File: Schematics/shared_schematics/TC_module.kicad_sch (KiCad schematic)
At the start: 12 parts, among them J7 Screw_Terminal_01x02

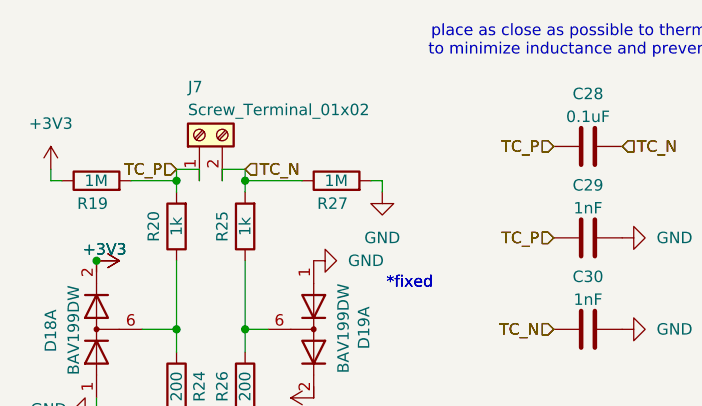
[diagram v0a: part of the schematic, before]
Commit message: organize working copy of lower valve board for merge to main
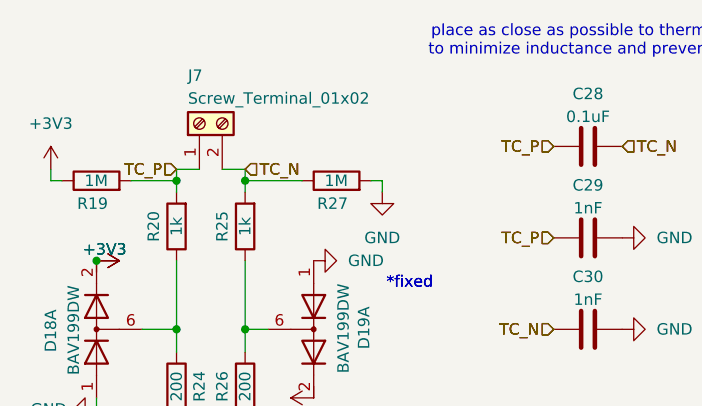
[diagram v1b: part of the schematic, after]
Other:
- moved on the sheet: J7
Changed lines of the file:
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@@
-	(wire
-		(pts
-			(xy 153.67 80.01) (xy 153.67 81.28)
-		)
-		(stroke
-			(width 0)
-			(type default)
-		)
-	)
-	(wire
-		(pts
-			(xy 151.13 80.01) (xy 151.13 81.28)
-		)
-		(stroke
-			(width 0)
-			(type default)
-		)
-	)
 	(wire
 		(pts
@@
 		(shape input)
 		(at 148.59 80.01 180)
-		(fields_autoplaced yes)
 		(effects
 			(font
@@
 		(shape input)
 		(at 190.5 77.47 180)
-		(fields_autoplaced yes)
 		(effects
 			(font
@@
 		(shape input)
 		(at 190.5 77.47 180)
-		(fields_autoplaced yes)
 		(effects
 			(font
@@
 		(shape input)
 		(at 148.59 114.3 180)
-		(fields_autoplaced yes)
 		(effects
 			(font
@@
 		(shape input)
 		(at 198.12 77.47 0)
-		(fields_autoplaced yes)
 		(effects
 			(font
@@
 		(shape input)
 		(at 190.5 87.63 180)
-		(fields_autoplaced yes)
 		(effects
 			(font
@@
 		(shape input)
 		(at 148.59 114.3 180)
-		(fields_autoplaced yes)
 		(effects
 			(font
@@
 		(shape input)
 		(at 190.5 97.79 180)
-		(fields_autoplaced yes)
 		(effects
 			(font
@@
 		(shape input)
 		(at 190.5 87.63 180)
-		(fields_autoplaced yes)
 		(effects
 			(font
@@
 		(shape input)
 		(at 148.59 80.01 180)
-		(fields_autoplaced yes)
 		(effects
 			(font
@@
 		(shape input)
 		(at 198.12 77.47 0)
-		(fields_autoplaced yes)
 		(effects
 			(font
@@
 		(shape input)
 		(at 156.21 80.01 0)
-		(fields_autoplaced yes)
 		(effects
 			(font
@@
 		(shape input)
 		(at 156.21 114.3 0)
-		(fields_autoplaced yes)
 		(effects
 			(font
@@
 		(shape input)
 		(at 190.5 97.79 180)
-		(fields_autoplaced yes)
 		(effects
 			(font
@@
 		(shape input)
 		(at 156.21 80.01 0)
-		(fields_autoplaced yes)
 		(effects
 			(font
@@
 		(shape input)
 		(at 156.21 114.3 0)
-		(fields_autoplaced yes)
 		(effects
 			(font
@@
 				)
 			)
-			(project ""
+			(project "lower_lc_board"
 				(path "/d63798c4-e363-437e-9012-e4aff32e6642/c6419db7-28a9-4bfa-8244-fc88166c795c/0f673b05-1261-4d55-8b13-e3d5496cfefa"
 					(reference "#PWR0118")
@@
 				)
 			)
-			(project ""
+			(project "lower_lc_board"
 				(path "/d63798c4-e363-437e-9012-e4aff32e6642/c6419db7-28a9-4bfa-8244-fc88166c795c/0f673b05-1261-4d55-8b13-e3d5496cfefa"
 					(reference "R26")
@@
 				)
 			)
-			(project ""
+			(project "lower_lc_board"
 				(path "/d63798c4-e363-437e-9012-e4aff32e6642/c6419db7-28a9-4bfa-8244-fc88166c795c/0f673b05-1261-4d55-8b13-e3d5496cfefa"
 					(reference "R24")
@@
 				)
 			)
-			(project ""
+			(project "lower_lc_board"
 				(path "/d63798c4-e363-437e-9012-e4aff32e6642/c6419db7-28a9-4bfa-8244-fc88166c795c/0f673b05-1261-4d55-8b13-e3d5496cfefa"
 					(reference "C32")
@@
 				)
 			)
-			(project ""
+			(project "lower_lc_board"
 				(path "/d63798c4-e363-437e-9012-e4aff32e6642/c6419db7-28a9-4bfa-8244-fc88166c795c/0f673b05-1261-4d55-8b13-e3d5496cfefa"
 					(reference "R27")
@@
 				)
 			)
-			(project ""
+			(project "lower_lc_board"
 				(path "/d63798c4-e363-437e-9012-e4aff32e6642/c6419db7-28a9-4bfa-8244-fc88166c795c/0f673b05-1261-4d55-8b13-e3d5496cfefa"
 					(reference "C31")
@@
 				)
 			)
-			(project ""
+			(project "lower_lc_board"
 				(path "/d63798c4-e363-437e-9012-e4aff32e6642/c6419db7-28a9-4bfa-8244-fc88166c795c/0f673b05-1261-4d55-8b13-e3d5496cfefa"
 					(reference "R40")
@@
 			)
 		)
-		(property "Datasheet" "${KIPRJMOD}/../../Documentation/diode_BAV16WS_DS.pdf"
+		(property "Datasheet" "${KIPRJMOD}/../../Datasheets/diode_BAV16WS_DS.pdf"
 			(at 163.83 97.79 0)
 			(effects
@@
 				)
 			)
-			(project ""
+			(project "lower_lc_board"
 				(path "/d63798c4-e363-437e-9012-e4aff32e6642/c6419db7-28a9-4bfa-8244-fc88166c795c/0f673b05-1261-4d55-8b13-e3d5496cfefa"
 					(reference "D18")
@@
 			)
 		)
-		(property "Datasheet" "${KIPRJMOD}/../../Documentation/diode_BAV16WS_DS.pdf"
+		(property "Datasheet" "${KIPRJMOD}/../../Datasheets/diode_BAV16WS_DS.pdf"
 			(at 139.7 97.79 0)
 			(effects
@@
 				)
 			)
-			(project ""
+			(project "lower_lc_board"
 				(path "/d63798c4-e363-437e-9012-e4aff32e6642/c6419db7-28a9-4bfa-8244-fc88166c795c/0f673b05-1261-4d55-8b13-e3d5496cfefa"
 					(reference "D18")
@@
 				)
 			)
-			(project ""
+			(project "lower_lc_board"
 				(path "/d63798c4-e363-437e-9012-e4aff32e6642/c6419db7-28a9-4bfa-8244-fc88166c795c/0f673b05-1261-4d55-8b13-e3d5496cfefa"
 					(reference "#PWR0114")
@@
 				)
 			)
-			(project ""
+			(project "lower_lc_board"
 				(path "/d63798c4-e363-437e-9012-e4aff32e6642/c6419db7-28a9-4bfa-8244-fc88166c795c/0f673b05-1261-4d55-8b13-e3d5496cfefa"
 					(reference "R29")
@@
 				)
 			)
-			(project ""
+			(project "lower_lc_board"
 				(path "/d63798c4-e363-437e-9012-e4aff32e6642/c6419db7-28a9-4bfa-8244-fc88166c795c/0f673b05-1261-4d55-8b13-e3d5496cfefa"
 					(reference "#PWR0120")
@@
 				)
 			)
-			(project ""
+			(project "lower_lc_board"
 				(path "/d63798c4-e363-437e-9012-e4aff32e6642/c6419db7-28a9-4bfa-8244-fc88166c795c/0f673b05-1261-4d55-8b13-e3d5496cfefa"
 					(reference "R28")
@@
 				)
 			)
-			(project ""
+			(project "lower_lc_board"
 				(path "/d63798c4-e363-437e-9012-e4aff32e6642/c6419db7-28a9-4bfa-8244-fc88166c795c/0f673b05-1261-4d55-8b13-e3d5496cfefa"
 					(reference "C30")
@@
 	(symbol
 		(lib_id "Connector:Screw_Terminal_01x02")
-		(at 151.13 76.2 90)
+		(at 151.13 74.93 90)
 		(unit 1)
 		(exclude_from_sim no)
@@
 		(dnp no)
 		(property "Reference" "J7"
-			(at 149.86 70.866 90)
+			(at 149.86 69.596 90)
 			(effects
 				(font
@@
 		)
 		(property "Value" "Screw_Terminal_01x02"
-			(at 149.86 73.406 90)
+			(at 149.86 72.136 90)
 			(effects
 				(font
@@
 		)
 		(property "Footprint" "TerminalBlock_TE-Connectivity:TerminalBlock_TE_282834-2_1x02_P2.54mm_Horizontal"
-			(at 151.13 76.2 0)
+			(at 151.13 74.93 0)
 			(effects
 				(font
@@
 		)
 		(property "Datasheet" "~"
-			(at 151.13 76.2 0)
+			(at 151.13 74.93 0)
 			(effects
 				(font
@@
 		)
 		(property "Description" "Generic screw terminal, single row, 01x02, script generated (kicad-library-utils/schlib/autogen/connector/)"
-			(at 151.13 76.2 0)
+			(at 151.13 74.93 0)
 			(effects
 				(font
@@
 		)
 		(property "Digikey" "ED10561-ND"
-			(at 151.13 76.2 90)
+			(at 151.13 74.93 90)
 			(effects
 				(font
@@
 				)
 			)
-			(project ""
+			(project "lower_lc_board"
 				(path "/d63798c4-e363-437e-9012-e4aff32e6642/c6419db7-28a9-4bfa-8244-fc88166c795c/0f673b05-1261-4d55-8b13-e3d5496cfefa"
 					(reference "J7")
@@
 				)
 			)
-			(project ""
+			(project "lower_lc_board"
 				(path "/d63798c4-e363-437e-9012-e4aff32e6642/c6419db7-28a9-4bfa-8244-fc88166c795c/0f673b05-1261-4d55-8b13-e3d5496cfefa"
 					(reference "#PWR0129")

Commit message: lower refactor for review
 - curr using horziontal screw for TC
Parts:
- C28: footprint Capacitor_SMD:C_0805_2012Metric -> Capacitor_SMD:C_0603_1608Metric; JLCPCB C49678 -> C14663
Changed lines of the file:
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@@
 		(shape input)
 		(at 148.59 80.01 180)
+		(fields_autoplaced yes)
 		(effects
 			(font
@@
 		(shape input)
 		(at 190.5 77.47 180)
+		(fields_autoplaced yes)
 		(effects
 			(font
@@
 		(shape input)
 		(at 190.5 77.47 180)
+		(fields_autoplaced yes)
 		(effects
 			(font
@@
 		(shape input)
 		(at 148.59 114.3 180)
+		(fields_autoplaced yes)
 		(effects
 			(font
@@
 		(shape input)
 		(at 198.12 77.47 0)
+		(fields_autoplaced yes)
 		(effects
 			(font
@@
 		(shape input)
 		(at 190.5 87.63 180)
+		(fields_autoplaced yes)
 		(effects
 			(font
@@
 		(shape input)
 		(at 148.59 114.3 180)
+		(fields_autoplaced yes)
 		(effects
 			(font
@@
 		(shape input)
 		(at 190.5 97.79 180)
+		(fields_autoplaced yes)
 		(effects
 			(font
@@
 		(shape input)
 		(at 190.5 87.63 180)
+		(fields_autoplaced yes)
 		(effects
 			(font
@@
 		(shape input)
 		(at 148.59 80.01 180)
+		(fields_autoplaced yes)
 		(effects
 			(font
@@
 		(shape input)
 		(at 198.12 77.47 0)
+		(fields_autoplaced yes)
 		(effects
 			(font
@@
 		(shape input)
 		(at 156.21 80.01 0)
+		(fields_autoplaced yes)
 		(effects
 			(font
@@
 		(shape input)
 		(at 156.21 114.3 0)
+		(fields_autoplaced yes)
 		(effects
 			(font
@@
 		(shape input)
 		(at 190.5 97.79 180)
+		(fields_autoplaced yes)
 		(effects
 			(font
@@
 		(shape input)
 		(at 156.21 80.01 0)
+		(fields_autoplaced yes)
 		(effects
 			(font
@@
 		(shape input)
 		(at 156.21 114.3 0)
+		(fields_autoplaced yes)
 		(effects
 			(font
@@
 					(unit 1)
 				)
-				(path "/d63798c4-e363-437e-9012-e4aff32e6642/c6419db7-28a9-4bfa-8244-fc88166c795c/a028da42-e7da-423c-a83c-32336e9b7a16"
-					(reference "#PWR0103")
-					(unit 1)
-				)
 			)
 		)
@@
 					(unit 1)
 				)
-				(path "/d63798c4-e363-437e-9012-e4aff32e6642/c6419db7-28a9-4bfa-8244-fc88166c795c/a028da42-e7da-423c-a83c-32336e9b7a16"
-					(reference "#PWR0110")
-					(unit 1)
-				)
 			)
 		)
@@
 					(unit 1)
 				)
-				(path "/d63798c4-e363-437e-9012-e4aff32e6642/c6419db7-28a9-4bfa-8244-fc88166c795c/a028da42-e7da-423c-a83c-32336e9b7a16"
-					(reference "R54")
-					(unit 1)
-				)
 			)
 		)
@@
 					(unit 1)
 				)
-				(path "/d63798c4-e363-437e-9012-e4aff32e6642/c6419db7-28a9-4bfa-8244-fc88166c795c/a028da42-e7da-423c-a83c-32336e9b7a16"
-					(reference "R55")
-					(unit 1)
-				)
 			)
 		)
@@
 					(unit 1)
 				)
-				(path "/d63798c4-e363-437e-9012-e4aff32e6642/c6419db7-28a9-4bfa-8244-fc88166c795c/a028da42-e7da-423c-a83c-32336e9b7a16"
-					(reference "C55")
-					(unit 1)
-				)
 			)
 		)
@@
 					(unit 1)
 				)
-				(path "/d63798c4-e363-437e-9012-e4aff32e6642/c6419db7-28a9-4bfa-8244-fc88166c795c/a028da42-e7da-423c-a83c-32336e9b7a16"
-					(reference "R59")
-					(unit 1)
-				)
 			)
 		)
@@
 					(unit 1)
 				)
-				(path "/d63798c4-e363-437e-9012-e4aff32e6642/c6419db7-28a9-4bfa-8244-fc88166c795c/a028da42-e7da-423c-a83c-32336e9b7a16"
-					(reference "#PWR0119")
-					(unit 1)
-				)
 			)
 		)
@@
 					(unit 1)
 				)
-				(path "/d63798c4-e363-437e-9012-e4aff32e6642/c6419db7-28a9-4bfa-8244-fc88166c795c/a028da42-e7da-423c-a83c-32336e9b7a16"
-					(reference "C54")
-					(unit 1)
-				)
 			)
 		)
@@
 					(unit 1)
 				)
-				(path "/d63798c4-e363-437e-9012-e4aff32e6642/c6419db7-28a9-4bfa-8244-fc88166c795c/a028da42-e7da-423c-a83c-32336e9b7a16"
-					(reference "R58")
-					(unit 1)
-				)
 			)
 		)
@@
 					(unit 2)
 				)
-				(path "/d63798c4-e363-437e-9012-e4aff32e6642/c6419db7-28a9-4bfa-8244-fc88166c795c/a028da42-e7da-423c-a83c-32336e9b7a16"
-					(reference "D9")
-					(unit 2)
-				)
 			)
 		)
@@
 					(unit 1)
 				)
-				(path "/d63798c4-e363-437e-9012-e4aff32e6642/c6419db7-28a9-4bfa-8244-fc88166c795c/a028da42-e7da-423c-a83c-32336e9b7a16"
-					(reference "D9")
-					(unit 1)
-				)
 			)
 		)
@@
 					(unit 1)
 				)
-				(path "/d63798c4-e363-437e-9012-e4aff32e6642/c6419db7-28a9-4bfa-8244-fc88166c795c/a028da42-e7da-423c-a83c-32336e9b7a16"
-					(reference "#PWR094")
-					(unit 1)
-				)
 			)
 		)
@@
 					(unit 1)
 				)
-				(path "/d63798c4-e363-437e-9012-e4aff32e6642/c6419db7-28a9-4bfa-8244-fc88166c795c/a028da42-e7da-423c-a83c-32336e9b7a16"
-					(reference "#PWR0138")
-					(unit 1)
-				)
 			)
 		)
@@
 					(unit 1)
 				)
-				(path "/d63798c4-e363-437e-9012-e4aff32e6642/c6419db7-28a9-4bfa-8244-fc88166c795c/a028da42-e7da-423c-a83c-32336e9b7a16"
-					(reference "R56")
-					(unit 1)
-				)
 			)
 		)
@@
 					(unit 1)
 				)
-				(path "/d63798c4-e363-437e-9012-e4aff32e6642/c6419db7-28a9-4bfa-8244-fc88166c795c/a028da42-e7da-423c-a83c-32336e9b7a16"
-					(reference "#PWR0100")
-					(unit 1)
-				)
 			)
 		)
@@
 					(unit 1)
 				)
-				(path "/d63798c4-e363-437e-9012-e4aff32e6642/c6419db7-28a9-4bfa-8244-fc88166c795c/a028da42-e7da-423c-a83c-32336e9b7a16"
-					(reference "#PWR098")
-					(unit 1)
-				)
 			)
 		)
@@
 					(unit 1)
 				)
-				(path "/d63798c4-e363-437e-9012-e4aff32e6642/c6419db7-28a9-4bfa-8244-fc88166c795c/a028da42-e7da-423c-a83c-32336e9b7a16"
-					(reference "R57")
-					(unit 1)
-				)
 			)
 		)
@@
 					(unit 1)
 				)
-				(path "/d63798c4-e363-437e-9012-e4aff32e6642/c6419db7-28a9-4bfa-8244-fc88166c795c/a028da42-e7da-423c-a83c-32336e9b7a16"
-					(reference "#PWR096")
-					(unit 1)
-				)
 			)
 		)
@@
 			)
 		)
-		(property "Footprint" "Capacitor_SMD:C_0805_2012Metric"
+		(property "Footprint" "Capacitor_SMD:C_0603_1608Metric"
 			(at 190.5 78.4352 0)
 			(effects
@@
 			)
 		)
-		(property "JLCPCB" "C49678"
+		(property "JLCPCB" "C14663"
 			(at 194.31 77.47 0)
 			(effects
@@
 				(path "/d63798c4-e363-437e-9012-e4aff32e6642/c6419db7-28a9-4bfa-8244-fc88166c795c/0f673b05-1261-4d55-8b13-e3d5496cfefa"
 					(reference "C30")
-					(unit 1)
-				)
-				(path "/d63798c4-e363-437e-9012-e4aff32e6642/c6419db7-28a9-4bfa-8244-fc88166c795c/a028da42-e7da-423c-a83c-32336e9b7a16"
-					(reference "C53")
 					(unit 1)
 				)
@@
 					(unit 1)
 				)
-				(path "/d63798c4-e363-437e-9012-e4aff32e6642/c6419db7-28a9-4bfa-8244-fc88166c795c/a028da42-e7da-423c-a83c-32336e9b7a16"
-					(reference "J11")
-					(unit 1)
-				)
 			)
 		)
@@
 					(unit 1)
 				)
-				(path "/d63798c4-e363-437e-9012-e4aff32e6642/c6419db7-28a9-4bfa-8244-fc88166c795c/a028da42-e7da-423c-a83c-32336e9b7a16"
-					(reference "#PWR0107")
-					(unit 1)
-				)

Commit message: update with new TC screw terminal
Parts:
- removed C29, C30: 1nF, Capacitor_SMD:C_0603_1608Metric, symbol Device:C
- J7: footprint TerminalBlock_TE-Connectivity:TerminalBlock_TE_282834-2_1x02_P2.54mm_Horizontal -> SCREW-VERT:1984769; Digikey ED10561-ND -> 277-1734-ND
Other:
- note added: "2026-03-27 - removed common mode TC filtering to accomodate for space with larger conn"

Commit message: update backplane orientation
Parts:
- J7: footprint SCREW-VERT:1984769 -> TerminalBlock_Phoenix:TerminalBlock_Phoenix_MPT-0,5-2-2.54_1x02_P2.54mm_Horizontal
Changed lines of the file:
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@@
+			)
+		)
+		(property "Sim.Device" ""
+			(at 139.7 81.28 0)
+			(effects
+				(font
+					(size 1.27 1.27)
+				)
+				(hide yes)
+			)
+		)
+		(property "Sim.Pins" ""
+			(at 139.7 81.28 0)
+			(effects
+				(font
+					(size 1.27 1.27)
+				)
+				(hide yes)
 			)
 		)
@@
 			)
 		)
+		(property "Sim.Device" ""
+			(at 148.59 86.36 0)
+			(effects
+				(font
+					(size 1.27 1.27)
+				)
+				(hide yes)
+			)
+		)
+		(property "Sim.Pins" ""
+			(at 148.59 86.36 0)
+			(effects
+				(font
+					(size 1.27 1.27)
+				)
+				(hide yes)
+			)
+		)
 		(pin "2"
 		)
@@
 			)
 		)
+		(property "Sim.Device" ""
+			(at 166.37 81.28 0)
+			(effects
+				(font
+					(size 1.27 1.27)
+				)
+				(hide yes)
+			)
+		)
+		(property "Sim.Pins" ""
+			(at 166.37 81.28 0)
+			(effects
+				(font
+					(size 1.27 1.27)
+				)
+				(hide yes)
+			)
+		)
 		(pin "1"
 		)
@@
 			)
 		)
+		(property "Sim.Device" ""
+			(at 156.21 104.14 0)
+			(effects
+				(font
+					(size 1.27 1.27)
+				)
+				(hide yes)
+			)
+		)
+		(property "Sim.Pins" ""
+			(at 156.21 104.14 0)
+			(effects
+				(font
+					(size 1.27 1.27)
+				)
+				(hide yes)
+			)
+		)
 		(pin "1"
 		)
@@
 			)
 		)
+		(property "Sim.Device" ""
+			(at 163.83 97.79 0)
+			(effects
+				(font
+					(size 1.27 1.27)
+				)
+				(hide yes)
+			)
+		)
+		(property "Sim.Pins" ""
+			(at 163.83 97.79 0)
+			(effects
+				(font
+					(size 1.27 1.27)
+				)
+				(hide yes)
+			)
+		)
 		(pin "6"
 		)
@@
 		)
 		(property "JLCPCB" "BAV199DW"
+			(at 139.7 97.79 0)
+			(effects
+				(font
+					(size 1.27 1.27)
+				)
+				(hide yes)
+			)
+		)
+		(property "Sim.Device" ""
+			(at 139.7 97.79 0)
+			(effects
+				(font
+					(size 1.27 1.27)
+				)
+				(hide yes)
+			)
+		)
+		(property "Sim.Pins" ""
 			(at 139.7 97.79 0)
 			(effects
@@
 			)
 		)
+		(property "Sim.Device" ""
+			(at 148.59 104.14 0)
+			(effects
+				(font
+					(size 1.27 1.27)
+				)
+				(hide yes)
+			)
+		)
+		(property "Sim.Pins" ""
+			(at 148.59 104.14 0)
+			(effects
+				(font
+					(size 1.27 1.27)
+				)
+				(hide yes)
+			)
+		)
 		(pin "1"
 		)
@@
 			)
 		)
+		(property "Sim.Device" ""
+			(at 156.21 86.36 0)
+			(effects
+				(font
+					(size 1.27 1.27)
+				)
+				(hide yes)
+			)
+		)
+		(property "Sim.Pins" ""
+			(at 156.21 86.36 0)
+			(effects
+				(font
+					(size 1.27 1.27)
+				)
+				(hide yes)
+			)
+		)
 		(pin "2"
 		)
@@
 			)
 		)
+		(property "Sim.Device" ""
+			(at 194.31 77.47 0)
+			(effects
+				(font
+					(size 1.27 1.27)
+				)
+				(hide yes)
+			)
+		)
+		(property "Sim.Pins" ""
+			(at 194.31 77.47 0)
+			(effects
+				(font
+					(size 1.27 1.27)
+				)
+				(hide yes)
+			)
+		)
 		(pin "2"
 		)
@@
 			)
 		)
-		(property "Footprint" "SCREW-VERT:1984769"
+		(property "Footprint" "TerminalBlock_Phoenix:TerminalBlock_Phoenix_MPT-0,5-2-2.54_1x02_P2.54mm_Horizontal"
 			(at 151.13 74.93 0)
 			(effects
@@
 			(effects
 				(font
+					(size 1.27 1.27)
+				)
+				(hide yes)
+			)
+		)
+		(property "Sim.Device" ""
+			(at 151.13 74.93 0)
+			(effects
+				(font
+					(size 1.27 1.27)
+				)
+				(hide yes)
+			)
+		)
+		(property "Sim.Pins" ""
+			(at 151.13 74.93 0)
+			(effects
+				(font

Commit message: WIP - i2c-2 refactor
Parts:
- C28: JLCPCB C14663 -> (none); LCSC (none) -> C14663
- D18, D19: JLCPCB BAV199DW -> (none)
- R19, R27: JLCPCB C22935 -> (none)
- R20, R25: JLCPCB C21190 -> (none)
- R24, R26: JLCPCB C8218 -> (none)
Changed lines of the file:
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@@
-			)
-		)
-		(property "JLCPCB" "C22935"
-			(at 139.7 81.28 0)
-			(effects
-				(font
-					(size 1.27 1.27)
-				)
-				(hide yes)
 			)
 		)
@@
 			)
 		)
-		(property "JLCPCB" "C21190"
-			(at 148.59 86.36 0)
-			(effects
-				(font
-					(size 1.27 1.27)
-				)
-				(hide yes)
-			)
-		)
 		(property "Sim.Device" ""
 			(at 148.59 86.36 0)
@@
 			)
 		)
-		(property "JLCPCB" "C22935"
-			(at 166.37 81.28 0)
-			(effects
-				(font
-					(size 1.27 1.27)
-				)
-				(hide yes)
-			)
-		)
 		(property "Sim.Device" ""
 			(at 166.37 81.28 0)
@@
 			)
 		)
-		(property "JLCPCB" "C8218"
-			(at 156.21 104.14 0)
-			(effects
-				(font
-					(size 1.27 1.27)
-				)
-				(hide yes)
-			)
-		)
 		(property "Sim.Device" ""
 			(at 156.21 104.14 0)
@@
 			)
 		)
-		(property "JLCPCB" "BAV199DW"
-			(at 163.83 97.79 0)
-			(effects
-				(font
-					(size 1.27 1.27)
-				)
-				(hide yes)
-			)
-		)
 		(property "Sim.Device" ""
 			(at 163.83 97.79 0)
@@
 		)
 		(property "LCSC" "C459846"
-			(at 139.7 97.79 0)
-			(effects
-				(font
-					(size 1.27 1.27)
-				)
-				(hide yes)
-			)
-		)
-		(property "JLCPCB" "BAV199DW"
 			(at 139.7 97.79 0)
 			(effects
@@
 			)
 		)
-		(property "JLCPCB" "C8218"
-			(at 148.59 104.14 0)
-			(effects
-				(font
-					(size 1.27 1.27)
-				)
-				(hide yes)
-			)
-		)
 		(property "Sim.Device" ""
 			(at 148.59 104.14 0)
@@
 			)
 		)
-		(property "JLCPCB" "C21190"
-			(at 156.21 86.36 0)
-			(effects
-				(font
-					(size 1.27 1.27)
-				)
-				(hide yes)
-			)
-		)
 		(property "Sim.Device" ""
 			(at 156.21 86.36 0)
@@
 			)
 		)
-		(property "JLCPCB" "C14663"
-			(at 194.31 77.47 0)
-			(effects
-				(font
-					(size 1.27 1.27)
-				)
-				(hide yes)
-			)
-		)
 		(property "Sim.Device" ""
 			(at 194.31 77.47 0)
@@
 			(at 194.31 77.47 0)
 			(effects
+				(font
+					(size 1.27 1.27)
+				)
+				(hide yes)
+			)
+		)
+		(property "LCSC" "C14663"
+			(at 194.31 77.47 0)
+			(effects
